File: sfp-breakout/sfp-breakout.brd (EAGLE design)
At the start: 65 x 65 mm, 40 parts, among them J1 694108106102, T1 BC847, T2 BC847, U1 LDO-MCP1825S, X1 PINHD-1X5LOCK, X2 PINHD-1X5LOCK, X3 PINHD-1X4LOCK

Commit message: sfp-breakout: X1 pin 5 missing connection to VCC_3V3
Due to an overisght, pin 5 of the X1 header was missing the intended
connection to the 3V3 plane.  Let's fix this.  No routing changes on the
PCB required, as this simply connects the VCC plane layer to the
through-hole.
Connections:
- net VCC_3V3: now also X1.5
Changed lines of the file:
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@@
 <wire x1="11.43" y1="16.9425" x2="11.43" y2="17.78" width="0.4064" layer="1"/>
 <via x="11.43" y="17.78" extent="1-16" drill="0.3"/>
+<contactref element="X1" pad="5"/>
 </signal>
 <signal name="TD_P" class="1">

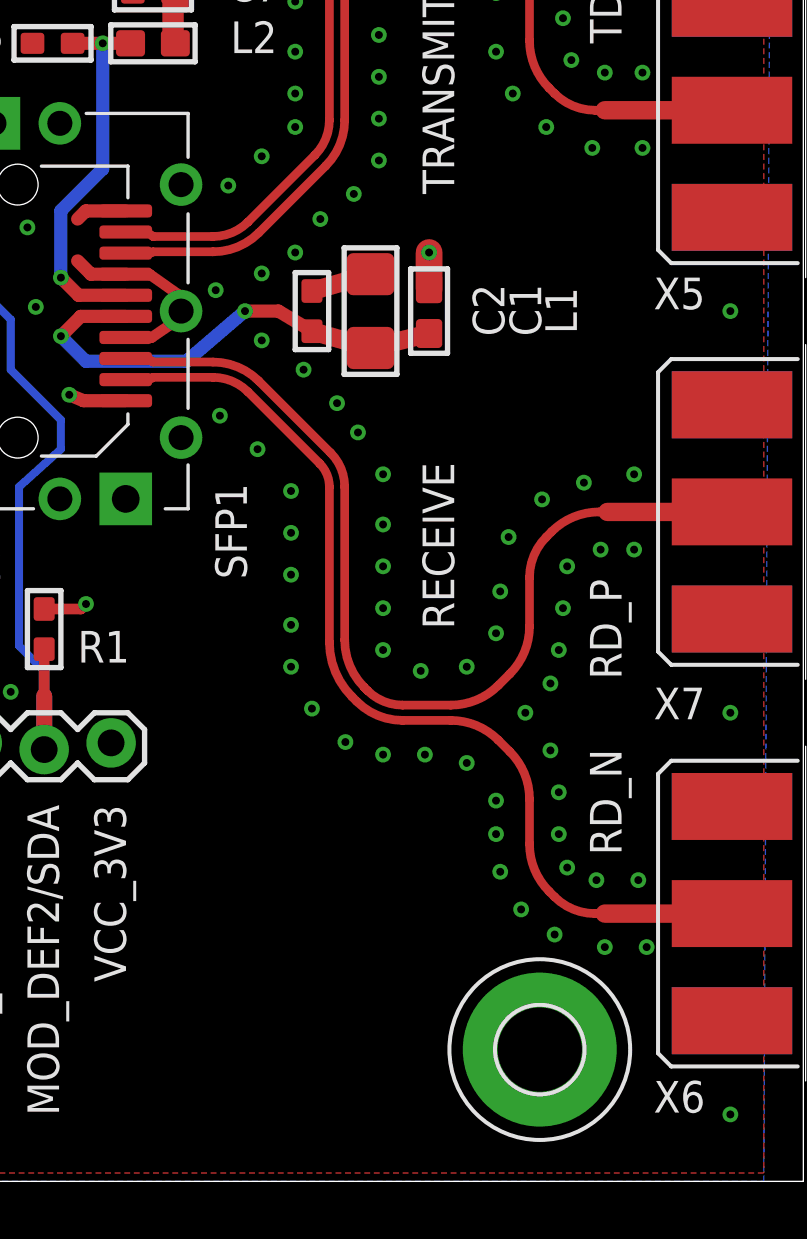
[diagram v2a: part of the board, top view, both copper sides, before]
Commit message: sfp-*: add OSHW logo, fill ext'd attribs for BOM
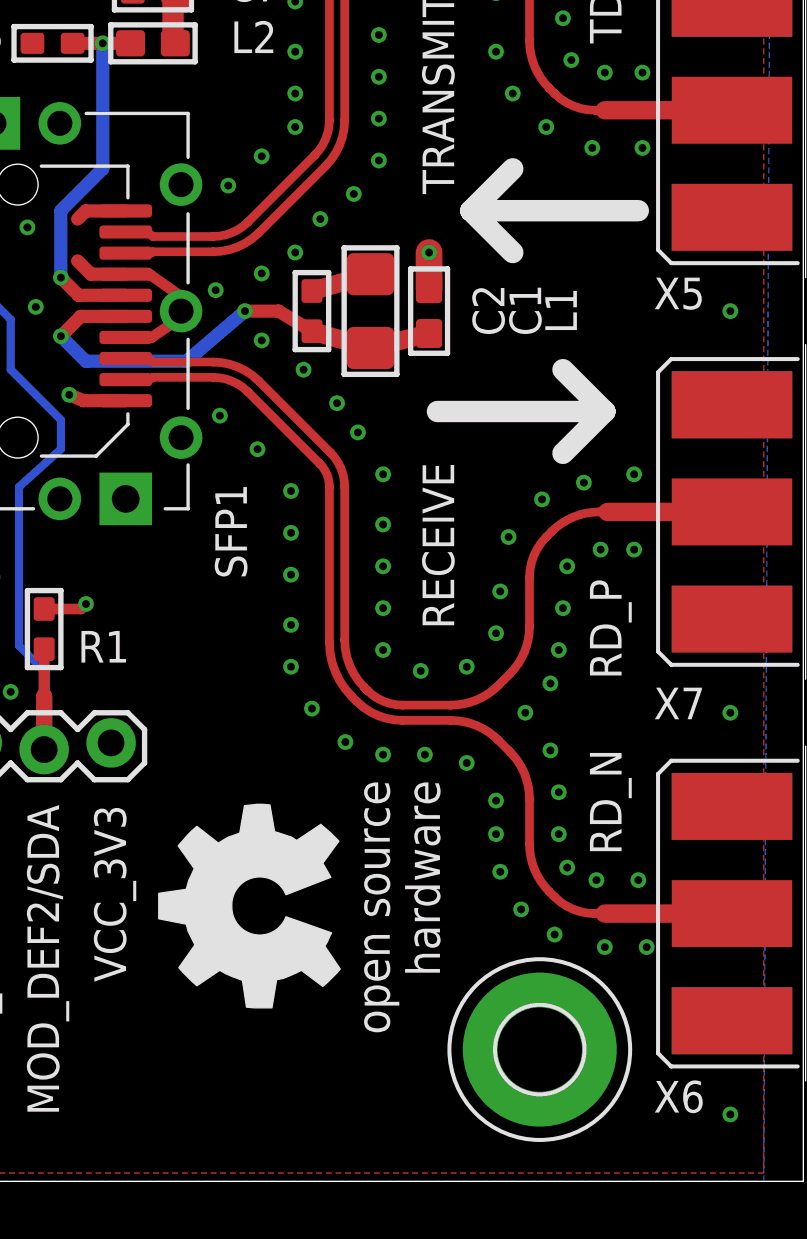
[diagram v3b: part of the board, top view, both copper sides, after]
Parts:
- added U$1: (no value), oshw:OSHW_8MM

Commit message: sfp-breakout: update BOM attribs for availability
... for next production run
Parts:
- D1: value SS16T3G -> MBRA160T3G
- J1: value 694108106102 -> PJ-002BH-SMT-TR

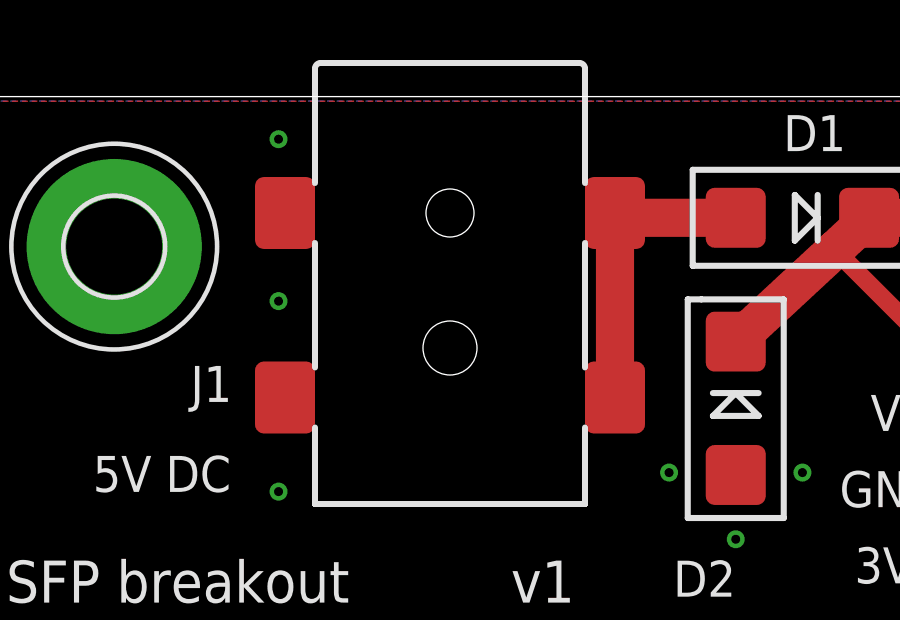
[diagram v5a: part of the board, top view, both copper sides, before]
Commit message: sfp-breakout: increase pad size for DC barrel conn
... as done for all recent projects for Kaempfe (by updating from the
resp. Wuerth lib)
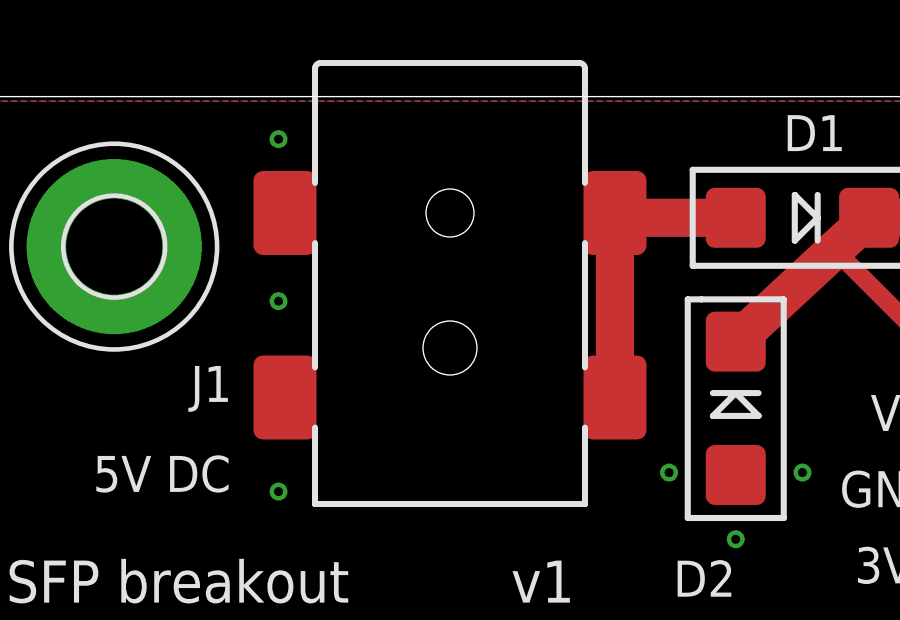
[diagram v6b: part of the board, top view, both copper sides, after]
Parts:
- J1: device sfp-breakout:694108106102 -> Wurth_Elektronik_Electromechanic_DC_Power_Jack_Connectors_rev15c:694108106102
